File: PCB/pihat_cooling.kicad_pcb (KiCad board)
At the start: 2 copper layers, 65 x 56 mm, 10 parts, among them M1 Fan, P1 Conn_02x20_Odd_Even

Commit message: update PCB
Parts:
- added C1: CP, Capacitor_THT:CP_Radial_D7.5mm_P2.50mm, F.Cu at (239.5, 145.6)
- added C2: CP, Capacitor_THT:CP_Radial_D7.5mm_P2.50mm, F.Cu at (204.1, 106.1)
- added C3: 100nF, Capacitor_SMD:C_0805_2012Metric, F.Cu at (249.5, 106.2)
- added C4: CP, Capacitor_THT:CP_Radial_D7.5mm_P2.50mm, F.Cu at (248.3, 129.6)
- added D1: 5V1, Diode_SMD:D_MiniMELF, F.Cu at (207.7, 137.7)
- added D10: LD_5V, LED_SMD:LED_1206_3216Metric, F.Cu at (211.0, 115.1)
- added D11: D4148, Diode_SMD:D_MiniMELF, F.Cu at (256.3, 105.2)
- added D2: 1N4007, Diode_SMD:D_SMA, F.Cu at (243.7, 137.6)
- added D3: 1N4007, Diode_SMD:D_SMA, F.Cu at (239.8, 137.6)
- added D6: 5V1, Diode_SMD:D_MiniMELF, F.Cu at (202.7, 133.4)
- added D7: 1N5820, Diode_SMD:D_SMA, F.Cu at (213.7, 143.8)
- added D8: LD_Thermal, LED_SMD:LED_1206_3216Metric, F.Cu at (211.0, 110.1)
- added D9: LED_12V, LED_SMD:LED_1206_3216Metric, F.Cu at (211.0, 112.7)
- added J1: Barrel_Jack, Connector_BarrelJack:BarrelJack_Wuerth_6941xx301002, F.Cu at (251.1, 137.8)
- added J2: Conn_01x03, Connector_PinHeader_2.54mm:PinHeader_1x03_P2.54mm_Vertical, F.Cu at (252.6, 108.0)
- added L1: 33uF, Inductor_SMD:L_Vishay_IHLP-2020, F.Cu at (213.7, 138.6)
- added Q1: AO3401A, Package_TO_SOT_SMD:SOT-23, F.Cu at (211.4, 133.6)
- added Q2: MMBT3906, Package_TO_SOT_SMD:SOT-23, F.Cu at (209.4, 127.8)
- added Q3: AO3401A, Package_TO_SOT_SMD:SOT-23, F.Cu at (208.3, 123.8)
- added Q4: MMBT3904, Package_TO_SOT_SMD:SOT-23, F.Cu at (248.4, 111.5)
- added R1: 100K, Diode_SMD:D_0805_2012Metric, F.Cu at (207.7, 142.4)
- added R10: 100, Diode_SMD:D_0805_2012Metric, F.Cu at (248.9, 114.6)
- added R11: 10K, Diode_SMD:D_0805_2012Metric, F.Cu at (251.9, 119.4)
- added R12: 10K, Diode_SMD:D_0805_2012Metric, F.Cu at (251.9, 123.1)
- added R2: 2K2, Diode_SMD:D_0805_2012Metric, F.Cu at (205.2, 132.5)
- added R3: 1K, Diode_SMD:D_0805_2012Metric, F.Cu at (207.5, 132.5)
- added R4: 100K, Diode_SMD:D_0805_2012Metric, F.Cu at (206.3, 127.9)
- added R5: 1K, Diode_SMD:D_0805_2012Metric, F.Cu at (211.6, 106.6)
- added R6: 1K, Diode_SMD:D_0805_2012Metric, F.Cu at (212.1, 118.3)
- added R7: 1K, Diode_SMD:D_0805_2012Metric, F.Cu at (209.7, 118.4)
- added R8: 100, Diode_SMD:D_0805_2012Metric, F.Cu at (259.7, 135.0)
- added R9: 100, Diode_SMD:D_0805_2012Metric, F.Cu at (262.7, 135.0)
- added REBOOT: Reboot, Button_Switch_THT:SW_PUSH_6mm, F.Cu at (257.1, 129.3)
- added SHUTDOWN: Shutdown, Button_Switch_THT:SW_PUSH_6mm, F.Cu at (257.1, 118.1)
- added TP1: TestPoint, TestPoint:TestPoint_Pad_D1.0mm, F.Cu at (236.3, 148.5)
- added TP2: TestPoint, TestPoint:TestPoint_Pad_D1.0mm, F.Cu at (202.0, 111.8)
- added TP3: TestPoint, TestPoint:TestPoint_Pad_D1.0mm, F.Cu at (246.7, 124.3)
- added U1: LM2596S-5, Package_TO_SOT_SMD:TO-263-5_TabPin3, F.Cu at (226.3, 143.3)
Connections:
- net +5V renamed +5VP
- P1 pad 10: /GPIO15(RXD0) -> (no net)
- P1 pad 11: /GPIO17(GEN0) -> /Thermal_Pin
- P1 pad 12: /GPIO18(GEN1)(PWM0) -> (no net)
- P1 pad 13: /GPIO27(GEN2) -> (no net)
- P1 pad 15: /GPIO22(GEN3) -> (no net)
- P1 pad 16: /GPIO23(GEN4) -> (no net)
- P1 pad 18: /GPIO24(GEN5) -> (no net)
- P1 pad 19: /GPIO10(SPI0_MOSI) -> (no net)
- P1 pad 21: /GPIO9(SPI0_MISO) -> (no net)
- P1 pad 22: /GPIO25(GEN6) -> (no net)
- P1 pad 23: /GPIO11(SPI0_SCK) -> (no net)
- P1 pad 24: /GPIO8(SPI0_CE_N) -> (no net)
- P1 pad 26: /GPIO7(SPI1_CE_N) -> (no net)
- P1 pad 27: /ID_SD -> (no net)
- P1 pad 28: /ID_SC -> (no net)
- P1 pad 29: /GPIO5 -> (no net)
- P1 pad 3: /GPIO2(SDA1) -> (no net)
- P1 pad 31: /GPIO6 -> (no net)
- P1 pad 32: /GPIO12(PWM0) -> (no net)
- P1 pad 33: /GPIO13(PWM1) -> /PWM_Pin
- P1 pad 35: /GPIO19(SPI1_MISO) -> (no net)
- P1 pad 36: /GPIO16 -> /Reboot_Pin
- P1 pad 37: /GPIO26 -> /Shutdown_Pin
- P1 pad 38: /GPIO20(SPI1_MOSI) -> (no net)
- P1 pad 40: /GPIO21(SPI1_SCK) -> (no net)
- P1 pad 5: /GPIO3(SCL1) -> (no net)
- P1 pad 7: /GPIO4(GCLK) -> (no net)
- P1 pad 8: /GPIO14(TXD0) -> (no net)
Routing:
- net +12V: track 0.00 -> 120.2 mm, vias 0 -> 1
- net +5VP: track 0.00 -> 90.4 mm
- net +5V: track 0.00 -> 81.4 mm, vias 0 -> 2
- net /Reboot_Pin: track 0.00 -> 49.7 mm
- net +3V3: track 0.00 -> 45.4 mm
- net Net-(D7-Pad1): track 0.00 -> 43.0 mm
- net /Shutdown_Pin: track 0.00 -> 27.5 mm
- net Net-(R8-Pad1): track 0.00 -> 23.3 mm
- net Net-(D1-Pad2): track 0.00 -> 20.6 mm
- net /Thermal_Pin: track 0.00 -> 15.4 mm
- net Net-(D2-Pad2): track 0.00 -> 13.4 mm
- net Net-(R9-Pad1): track 0.00 -> 12.5 mm
- net Net-(D1-Pad1): track 0.00 -> 11.8 mm
- net Net-(D11-Pad1): track 0.00 -> 10.7 mm
- net Net-(Q2-Pad3): track 0.00 -> 10.4 mm
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- added copper zone on B.Cu, net GND
- added copper zone on F.Cu, net GND
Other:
- outline, holes or cut-outs redrawn
- net class Default: clearance 0.2032 -> 0.3048; trace_width 0.254 -> 0.3556
- rule trace_clearance: 0.2032 -> 0.3048
- board text removed: "CAMERA"

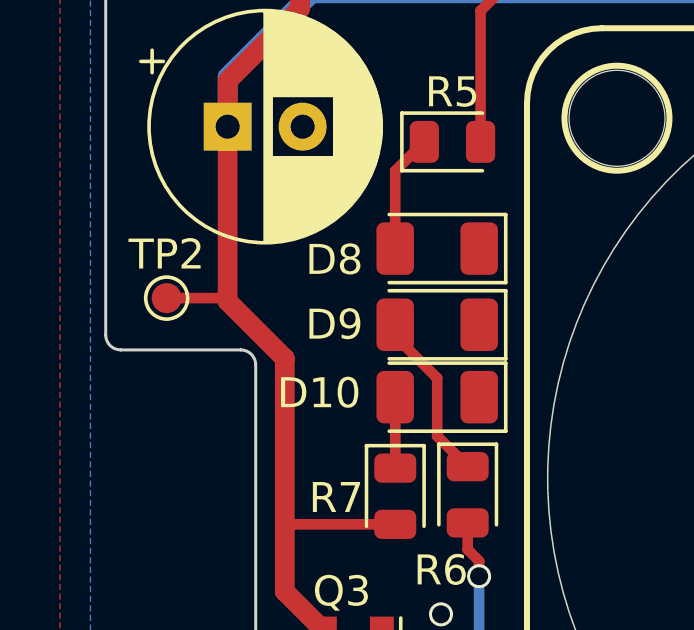
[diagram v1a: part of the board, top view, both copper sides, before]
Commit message: change LED fsilk
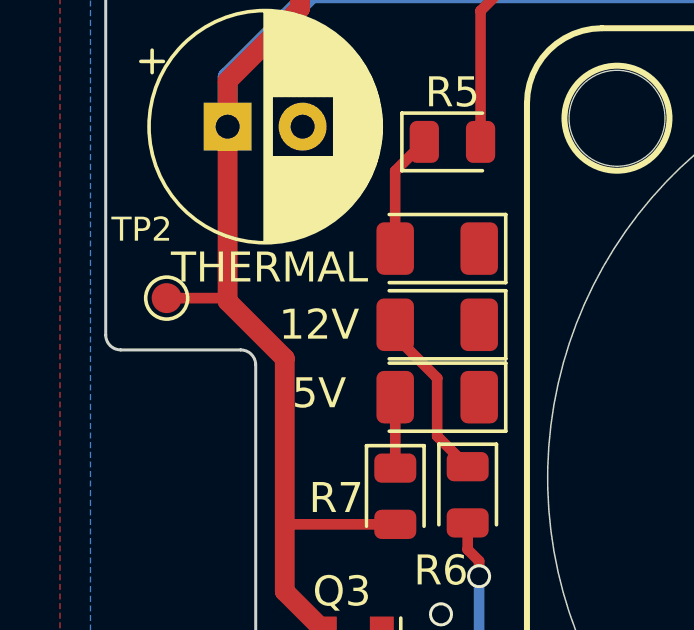
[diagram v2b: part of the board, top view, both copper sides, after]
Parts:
- renumbered D9 to 12V, D10 to 5V, D8 to THERMAL
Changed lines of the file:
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@@
     (tags diode)
     (attr smd)
-    (fp_text reference D10 (at 3.937 0.127) (layer F.SilkS)
+    (fp_text reference 5V (at 3.937 0.127) (layer F.SilkS)
       (effects (font (size 1 1) (thickness 0.15)))
     )
@@
     (tags diode)
     (attr smd)
-    (fp_text reference D9 (at 3.429 0) (layer F.SilkS)
+    (fp_text reference 12V (at 3.937 0) (layer F.SilkS)
       (effects (font (size 1 1) (thickness 0.15)))
     )
@@
     (tags diode)
     (attr smd)
-    (fp_text reference D8 (at 3.429 -0.381) (layer F.SilkS)
+    (fp_text reference THERMAL (at 5.588 -0.635) (layer F.SilkS)
       (effects (font (size 1 1) (thickness 0.15)))
     )
@@
     (tags "test point SMD pad")
     (attr virtual)
-    (fp_text reference TP2 (at 0 -1.448) (layer F.SilkS)
-      (effects (font (size 1 1) (thickness 0.15)))
+    (fp_text reference TP2 (at -0.8255 -2.286) (layer F.SilkS)
+      (effects (font (size 0.8 0.8) (thickness 0.15)))
     )
     (fp_text value TestPoint (at 0 1.55) (layer F.Fab)

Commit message: update fsilks
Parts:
- moved TP2 12.1 mm to (210.0, 102.7)
- moved C2 1.08 mm to (204.1, 105.0)
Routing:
- net +5VP: track 90.4 -> 91.1 mm
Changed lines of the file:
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@@
     (thickness 1.6)
     (drawings 35)
-    (tracks 227)
+    (tracks 228)
     (zones 0)
     (modules 48)
@@
     (attr smd)
     (fp_text reference R10 (at -3.302 0) (layer F.SilkS)
-      (effects (font (size 1 1) (thickness 0.15)))
+      (effects (font (size 0.8 0.8) (thickness 0.15)))
     )
     (fp_text value 100 (at 0 1.65) (layer F.Fab)
@@
     (attr smd)
     (fp_text reference R9 (at 2.54 0 180) (layer F.SilkS)
-      (effects (font (size 1 1) (thickness 0.15)))
+      (effects (font (size 0.8 0.8) (thickness 0.15)))
     )
     (fp_text value 100 (at 0 1.65 90) (layer F.Fab)
@@
     (attr smd)
     (fp_text reference R8 (at 2.4915 0.127 180) (layer F.SilkS)
-      (effects (font (size 1 1) (thickness 0.15)))
+      (effects (font (size 0.8 0.8) (thickness 0.15)))
     )
     (fp_text value 100 (at 0 1.65 90) (layer F.Fab)
@@
     (attr smd)
     (fp_text reference R7 (at 0.0635 1.9685 180) (layer F.SilkS)
-      (effects (font (size 1 1) (thickness 0.15)))
+      (effects (font (size 0.8 0.8) (thickness 0.15)))
     )
     (fp_text value 1K (at 0 1.65 90) (layer F.Fab)
@@
     (attr smd)
     (fp_text reference R6 (at 2.525 0.889 180) (layer F.SilkS)
-      (effects (font (size 1 1) (thickness 0.15)))
+      (effects (font (size 0.8 0.8) (thickness 0.15)))
     )
     (fp_text value 1K (at 0 1.65 90) (layer F.Fab)
@@
     (attr smd)
     (fp_text reference R5 (at 0 -1.65) (layer F.SilkS)
-      (effects (font (size 1 1) (thickness 0.15)))
+      (effects (font (size 0.8 0.8) (thickness 0.15)))
     )
     (fp_text value 1K (at 0 1.65) (layer F.Fab)
@@
     (attr smd)
     (fp_text reference D11 (at 3.556 1.778 180) (layer F.SilkS)
-      (effects (font (size 1 1) (thickness 0.15)))
+      (effects (font (size 0.8 0.8) (thickness 0.15)))
     )
     (fp_text value D4148 (at 0 1.75 90) (layer F.Fab)
@@
     (tags diode)
     (attr smd)
-    (fp_text reference 5V (at 3.937 0.127) (layer F.SilkS)
-      (effects (font (size 1 1) (thickness 0.15)))
+    (fp_text reference 5V (at 3.6195 0) (layer F.SilkS)
+      (effects (font (size 1.1 1.1) (thickness 0.17)))
     )
     (fp_text value LD_5V (at 0 1.82) (layer F.Fab)
@@
     (attr smd)
     (fp_text reference 12V (at 3.937 0) (layer F.SilkS)
-      (effects (font (size 1 1) (thickness 0.15)))
+      (effects (font (size 1.1 1.1) (thickness 0.17)))
     )
     (fp_text value LED_12V (at 0 1.82) (layer F.Fab)
@@
     (tags diode)
     (attr smd)
-    (fp_text reference THERMAL (at 5.588 -0.635) (layer F.SilkS)
-      (effects (font (size 1 1) (thickness 0.15)))
+    (fp_text reference THERMAL (at 6.0325 -0.0635) (layer F.SilkS)
+      (effects (font (size 1.1 1.1) (thickness 0.17)))
     )
     (fp_text value LD_Thermal (at 0 1.82) (layer F.Fab)
@@
     (attr smd)
     (fp_text reference D3 (at 3.302 -2.921 180) (layer F.SilkS)
-      (effects (font (size 1 1) (thickness 0.15)))
+      (effects (font (size 0.8 0.8) (thickness 0.15)))
     )
     (fp_text value 1N4007 (at 0 2.6 90) (layer F.Fab)
@@
     (attr smd)
     (fp_text reference D2 (at 4.318 1.143 180) (layer F.SilkS)
-      (effects (font (size 1 1) (thickness 0.15)))
+      (effects (font (size 0.8 0.8) (thickness 0.15)))
     )
     (fp_text value 1N4007 (at 0 2.6 90) (layer F.Fab)
@@
     (tags "inductor vishay ihlp smd")
     (attr smd)
-    (fp_text reference L1 (at 0 -3.54 180) (layer F.SilkS)
+    (fp_text reference L1 (at 1.0795 -3.683 180) (layer F.SilkS)
       (effects (font (size 1 1) (thickness 0.15)))
     )
@@
   )
   (module TestPoint:TestPoint_Pad_D1.0mm (layer F.Cu)
-    (at 202.032 111.773)
+    (at 209.9695 102.6925)
     (descr "SMD pad as test Point, diameter 1.0mm")
     (tags "test point SMD pad")
     (attr virtual)
-    (fp_text reference TP2 (at -0.8255 -2.286) (layer F.SilkS)
+    (fp_text reference TP2 (at -0.508 -1.5875) (layer F.SilkS)
       (effects (font (size 0.8 0.8) (thickness 0.15)))
     )
@@
     (attr smd)
     (fp_text reference Q4 (at -0.254 -3.048 180) (layer F.SilkS)
-      (effects (font (size 1 1) (thickness 0.15)))
+      (effects (font (size 0.8 0.8) (thickness 0.15)))
     )
     (fp_text value MMBT3904 (at 0 2.5 90) (layer F.Fab)
@@
     (attr smd)
     (fp_text reference Q3 (at -2.286 0.381 180) (layer F.SilkS)
-      (effects (font (size 1 1) (thickness 0.15)))
+      (effects (font (size 0.8 0.8) (thickness 0.15)))
     )
     (fp_text value AO3401A (at 0 2.5 90) (layer F.Fab)
@@
     (attr smd)
     (fp_text reference Q2 (at 0.508 2.794 180) (layer F.SilkS)
-      (effects (font (size 1 1) (thickness 0.15)))
+      (effects (font (size 0.8 0.8) (thickness 0.15)))
     )
     (fp_text value MMBT3906 (at 0 2.5 90) (layer F.Fab)
@@
     (attr smd)
     (fp_text reference Q1 (at -2.667 0 180) (layer F.SilkS)
-      (effects (font (size 1 1) (thickness 0.15)))
+      (effects (font (size 0.8 0.8) (thickness 0.15)))
     )
     (fp_text value AO3401A (at 0 2.5 90) (layer F.Fab)
@@
     (tags "Through hole pin header THT 1x03 2.54mm single row")
     (fp_text reference J2 (at 0 -2.33) (layer F.SilkS)
-      (effects (font (size 1 1) (thickness 0.15)))
+      (effects (font (size 0.8 0.8) (thickness 0.15)))
     )
     (fp_text value Conn_01x03 (at 0 7.41) (layer F.Fab)
@@
   )
   (module Capacitor_THT:CP_Radial_D7.5mm_P2.50mm (layer F.Cu)
-    (at 204.064 106.058)
+    (at 204.064 104.9785)
     (descr "CP, Radial series, Radial, pin pitch=2.50mm, , diameter=7.5mm, Electrolytic Capacitor")
     (tags "CP Radial series Radial pin pitch 2.50mm  diameter 7.5mm Electrolytic Capacitor")
-    (fp_text reference C2 (at 1.25 -5) (layer F.SilkS)
+    (fp_text reference C2 (at -2.921 -3.6195) (layer F.SilkS)
       (effects (font (size 1 1) (thickness 0.15)))
     )
@@
   (segment (start 204.064 104.534) (end 206.477 102.121) (width 0.6604) (layer F.Cu) (net 5))
   (segment (start 203.958433 111.773) (end 204.064 111.878567) (width 0.3556) (layer F.Cu) (net 5))
-  (segment (start 202.032 111.773) (end 203.958433 111.773) (width 0.3556) (layer F.Cu) (net 5))
   (segment (start 206.0475 119.3145) (end 205.969 119.393) (width 0.3556) (layer F.Cu) (net 5))
   (segment (start 209.652 119.3145) (end 206.0475 119.3145) (width 0.3556) (layer F.Cu) (net 5))
@@
   (segment (start 251.308 102.883) (end 250.038 101.613) (width 0.6604) (layer B.Cu) (net 5))
   (segment (start 250.038 101.613) (end 206.858 101.613) (width 0.6604) (layer B.Cu) (net 5))
-  (segment (start 204.064 104.407) (end 204.064 106.058) (width 0.6604) (layer B.Cu) (net 5))
   (segment (start 206.858 101.613) (end 204.064 104.407) (width 0.6604) (layer B.Cu) (net 5))
+  (segment (start 204.064 104.9785) (end 204.064 104.407) (width 0.6604) (layer B.Cu) (net 5))
+  (segment (start 207.0485 102.6925) (end 206.477 102.121) (width 0.3556) (layer F.Cu) (net 5))
+  (segment (start 209.9695 102.6925) (end 207.0485 102.6925) (width 0.3556) (layer F.Cu) (net 5))
   (segment (start 210.48 128.907) (end 210.348 128.775) (width 0.6604) (layer F.Cu) (net 6))
   (segment (start 210.48 132.617) (end 210.48 128.907) (width 0.6604) (layer F.Cu) (net 6))
